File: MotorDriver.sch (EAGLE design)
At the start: 2 parts, among them IC1 L293E, IC2 74HC14N

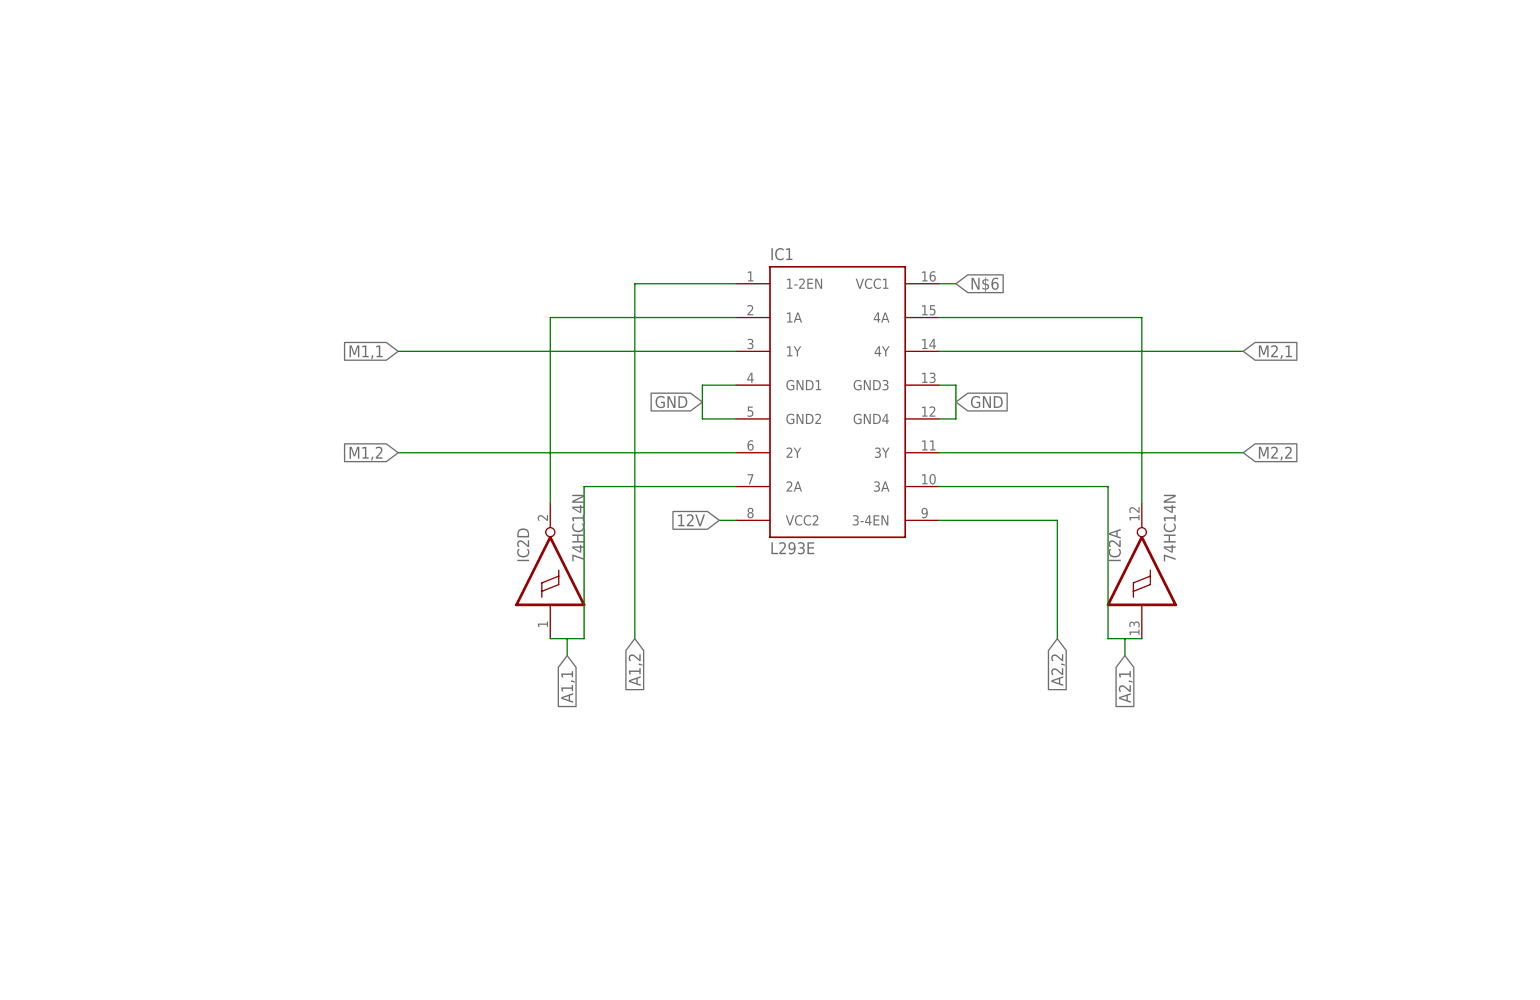
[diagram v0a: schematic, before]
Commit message: Added fly-back diodes
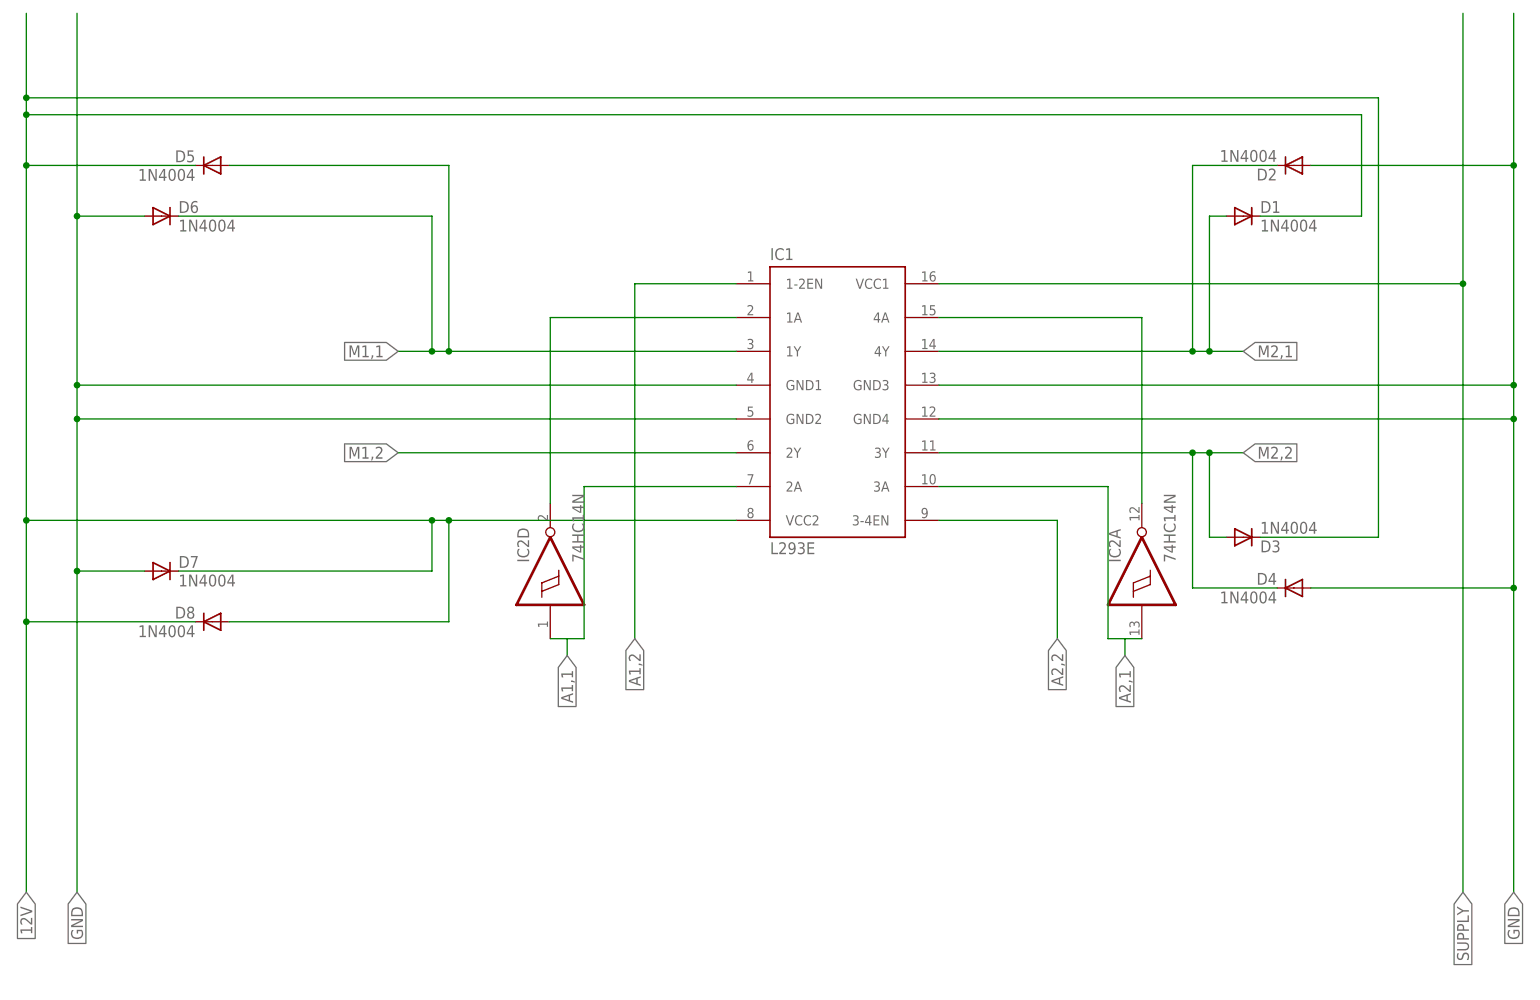
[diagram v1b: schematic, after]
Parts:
- added D1, D2, D3, D4, D5, D6, D7, D8: 1N4004, diode:1N4004
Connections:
- net N$6 renamed SUPPLY
- net 12V: now also D1.C, D3.C, D5.C, D7.C, D8.A, D8.C
- net GND: now also D2.A, D4.A, D6.A, D7.A
- net M1,1: now also D5.A, D6.C
- net M2,1: now also D1.A, D2.C
- net M2,2: now also D3.A, D4.C
